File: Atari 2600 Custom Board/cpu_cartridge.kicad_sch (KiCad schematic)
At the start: 8 parts, among them SW1 B3F-4050

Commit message: Cleaned up electrical rules violations
Cleaned up electrical rules violations
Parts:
- removed CRT1: ~, symbol 1_atari_library:EBC12DCWN
- removed SW1: B3F-4050, SW_B3F-4050_OMR, symbol 1_atari_library:B3F-4050
- removed U1: ~, symbol 1_atari_library:6507
- added CRT2: ~, symbol Atari2600_Library:EBC12DCWN
- added SW8: B3F-4050, SW_B3F-4050_OMR, symbol Atari2600_Library:B3F-4050
- added U5: ~, symbol Atari2600_Library:6507
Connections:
- net A0: now also CRT2.8 (A0), U5.5 (A0)
- net A1: now also CRT2.7 (A1), U5.6 (A1)
- net A10: now also CRT2.19 (A10), U5.15 (A10)
- net A11: now also CRT2.20 (A11), U5.16 (A11)
- net A12: now also CRT2.18 (A12), U5.17 (A12)
- net A2: now also CRT2.6 (A2), U5.7 (A2)
- net A3: now also CRT2.5 (A3), U5.8 (A3)
- net A4: now also CRT2.4 (A4), U5.9 (A4)
- net A5: now also CRT2.3 (A5), U5.10 (A5)
- net A6: now also CRT2.2 (A6), U5.11 (A6)
- net A7: now also CRT2.1 (A7), U5.12 (A7)
- net A8: now also CRT2.22 (A8), U5.13 (A8)
- net A9: now also CRT2.21 (A9), U5.14 (A9)
- net CPU_RW: now also U5.26 (R/~{W})
- net D0: now also CRT2.9 (D0), U5.25 (D0)
- net D1: now also CRT2.10 (D1), U5.24 (D1)
- net D2: now also CRT2.11 (D2), U5.23 (D2)
- net D3: now also CRT2.13 (D3), U5.22 (D3)
- net D4: now also CRT2.14 (D4), U5.21 (D4)
- net D5: now also CRT2.15 (D5), U5.20 (D5)
- net D6: now also CRT2.16 (D6), U5.19 (D6)
- net D7: now also CRT2.17 (D7), U5.18 (D7)
- net GND: now also CRT2.12 (GND), CRT2.24 (SGND), SW8.1, SW8.3, U5.2 (GND)
- net READY: now also U5.3 (RDY)
- net VCC: now also CRT2.23 (+5V), SW8.2, SW8.4, U5.1 (~{RES}), U5.4 (VCC)
- new net PHI_0: U5.27 (PHI_0)
- new net PHI_2: U5.28 (PHI_2)

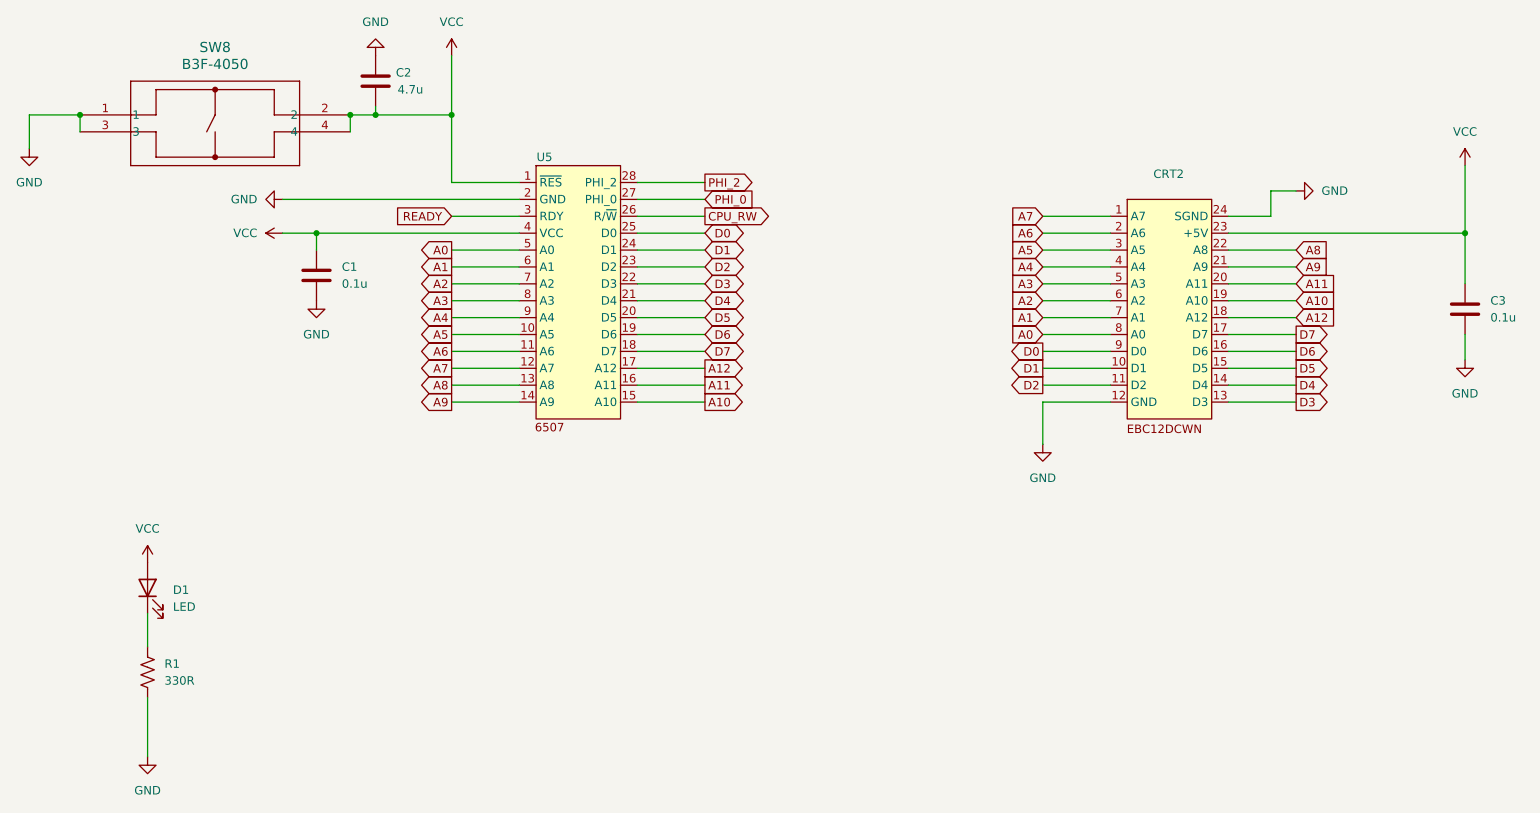
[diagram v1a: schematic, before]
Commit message: Fixed some incorrect values and re-annotated
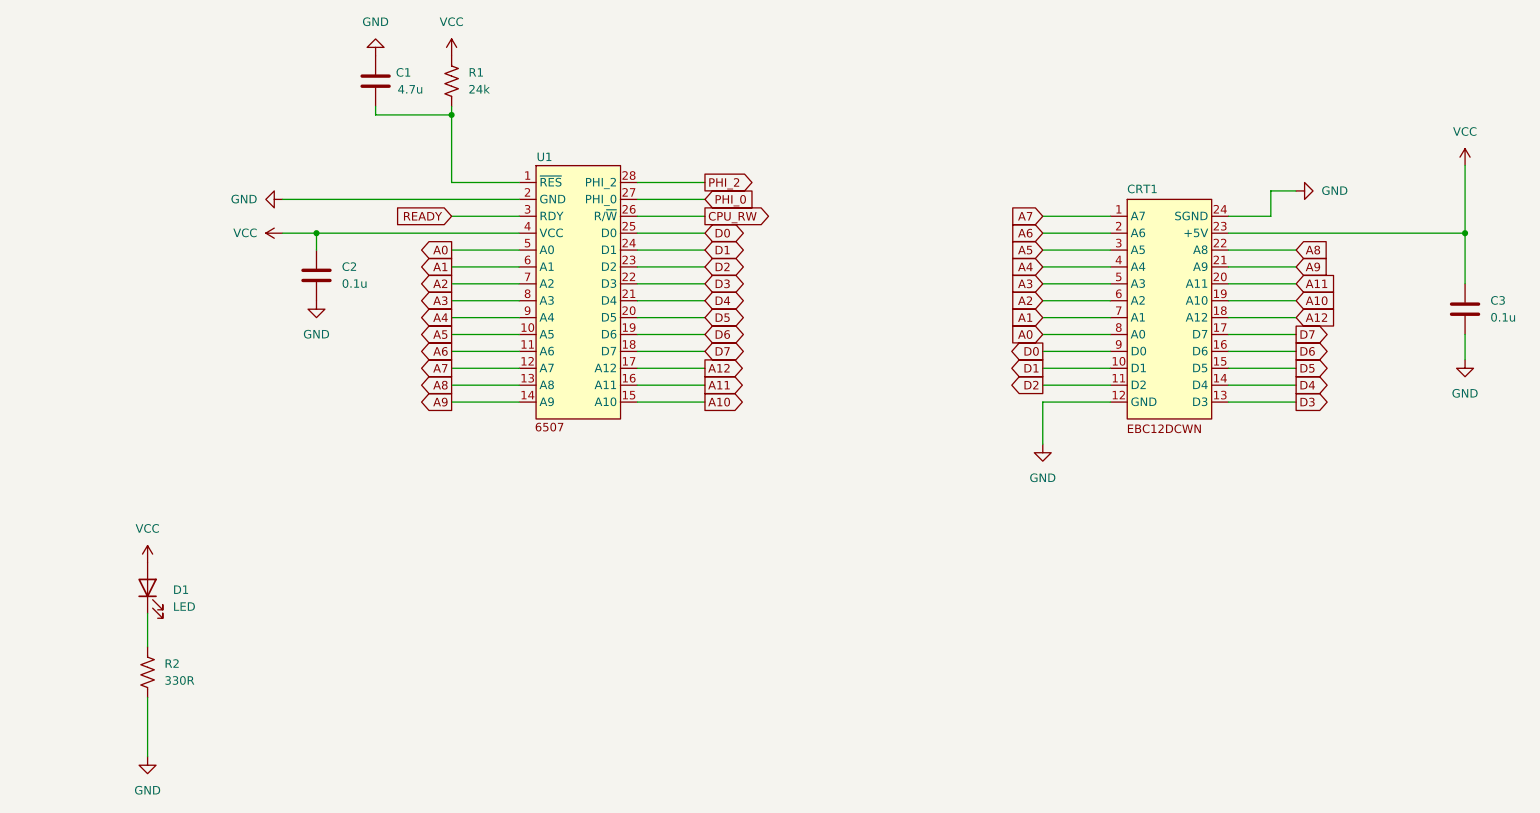
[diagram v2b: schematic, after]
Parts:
- removed SW8: B3F-4050, SW_B3F-4050_OMR, symbol Atari2600_Library:B3F-4050
- added R1: 24k, Resistor_SMD:R_0805_2012Metric_Pad1.20x1.40mm_HandSolder, symbol Device:R_US
- renumbered C2 to C1, C1 to C2, CRT2 to CRT1, R1 to R2, U5 to U1
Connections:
- net VCC: now also R1.1; no longer C1.2, U1.1 (~{RES})
- new net: C1.2, R1.2, U1.1 (~{RES})

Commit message: assign footprints
assigned most footprints to schematic
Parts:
- C1, C2, C3: footprint (none) -> Capacitor_SMD:C_0805_2012Metric_Pad1.18x1.45mm_HandSolder
- CRT1: footprint (none) -> Atari2600_Libary:J200-CatridgeConn
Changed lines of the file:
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@@
 			)
 		)
-		(property "Footprint" ""
+		(property "Footprint" "Capacitor_SMD:C_0805_2012Metric_Pad1.18x1.45mm_HandSolder"
 			(at 257.5052 92.71 0)
 			(effects
@@
 			)
 		)
-		(property "Footprint" ""
+		(property "Footprint" "Atari2600_Libary:J200-CatridgeConn"
 			(at 208.28 71.12 0)
 			(effects
@@
 			)
 		)
-		(property "Footprint" ""
+		(property "Footprint" "Capacitor_SMD:C_0805_2012Metric_Pad1.18x1.45mm_HandSolder"
 			(at 93.6752 58.42 0)
 			(effects
@@
 			)
 		)
-		(property "Footprint" ""
+		(property "Footprint" "Capacitor_SMD:C_0805_2012Metric_Pad1.18x1.45mm_HandSolder"
 			(at 84.7852 87.63 0)
 			(effects

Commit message: Change footprintf to regular 0805
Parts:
- C1, C2, C3: footprint Capacitor_SMD:C_0805_2012Metric_Pad1.18x1.45mm_HandSolder -> Capacitor_SMD:C_0805_2012Metric
- D1: footprint Diode_SMD:D_MiniMELF_Handsoldering -> Diode_SMD:D_0805_2012Metric
- R1, R2: footprint Resistor_SMD:R_0805_2012Metric_Pad1.20x1.40mm_HandSolder -> Resistor_SMD:R_0805_2012Metric
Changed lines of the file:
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@@
 			)
 		)
-		(property "Footprint" "Capacitor_SMD:C_0805_2012Metric_Pad1.18x1.45mm_HandSolder"
+		(property "Footprint" "Capacitor_SMD:C_0805_2012Metric"
 			(at 257.5052 92.71 0)
 			(effects
@@
 			)
 		)
-		(property "Footprint" "Diode_SMD:D_MiniMELF_Handsoldering"
+		(property "Footprint" "Diode_SMD:D_0805_2012Metric"
 			(at 58.42 130.81 0)
 			(effects
@@
 			)
 		)
-		(property "Footprint" "Resistor_SMD:R_0805_2012Metric_Pad1.20x1.40mm_HandSolder"
+		(property "Footprint" "Resistor_SMD:R_0805_2012Metric"
 			(at 105.156 54.864 90)
 			(effects
@@
 			)
 		)
-		(property "Footprint" "Resistor_SMD:R_0805_2012Metric_Pad1.20x1.40mm_HandSolder"
+		(property "Footprint" "Resistor_SMD:R_0805_2012Metric"
 			(at 59.436 143.764 90)
 			(effects
@@
 			)
 		)
-		(property "Footprint" "Capacitor_SMD:C_0805_2012Metric_Pad1.18x1.45mm_HandSolder"
+		(property "Footprint" "Capacitor_SMD:C_0805_2012Metric"
 			(at 93.6752 58.42 0)
 			(effects
@@
 			)
 		)
-		(property "Footprint" "Capacitor_SMD:C_0805_2012Metric_Pad1.18x1.45mm_HandSolder"
+		(property "Footprint" "Capacitor_SMD:C_0805_2012Metric"
 			(at 84.7852 87.63 0)
 			(effects
